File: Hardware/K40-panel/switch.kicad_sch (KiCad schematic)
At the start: 2 parts

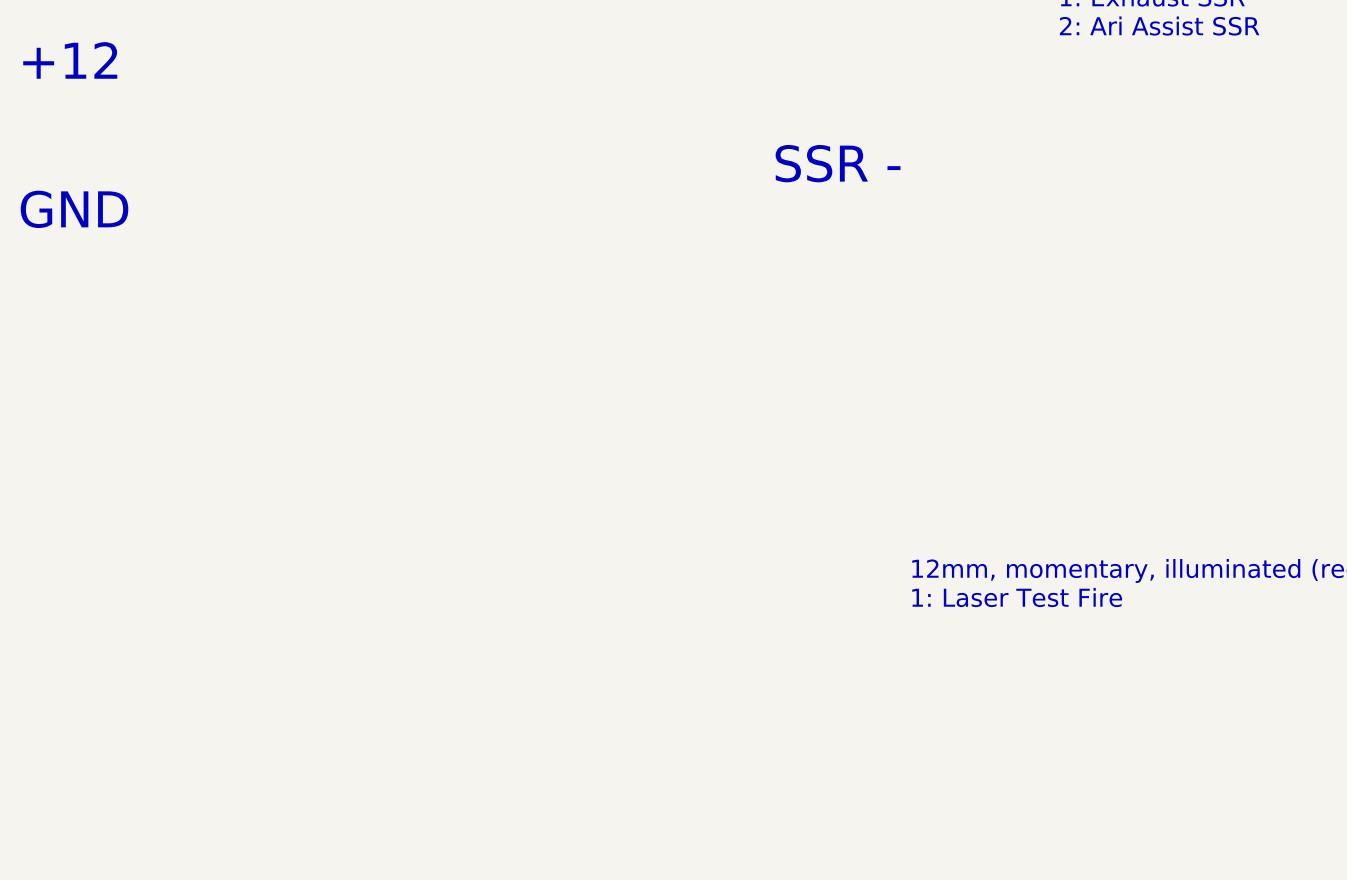
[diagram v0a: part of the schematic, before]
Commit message: modified:   Hardware/K40-panel/K40-panel.kicad_sch 	modified:   Hardware/K40-panel/switch.kicad_sch Updated labels 	modified:   Hardware/K40-power/K40-power.kicad_sch CLeaned up auxillary power diagram
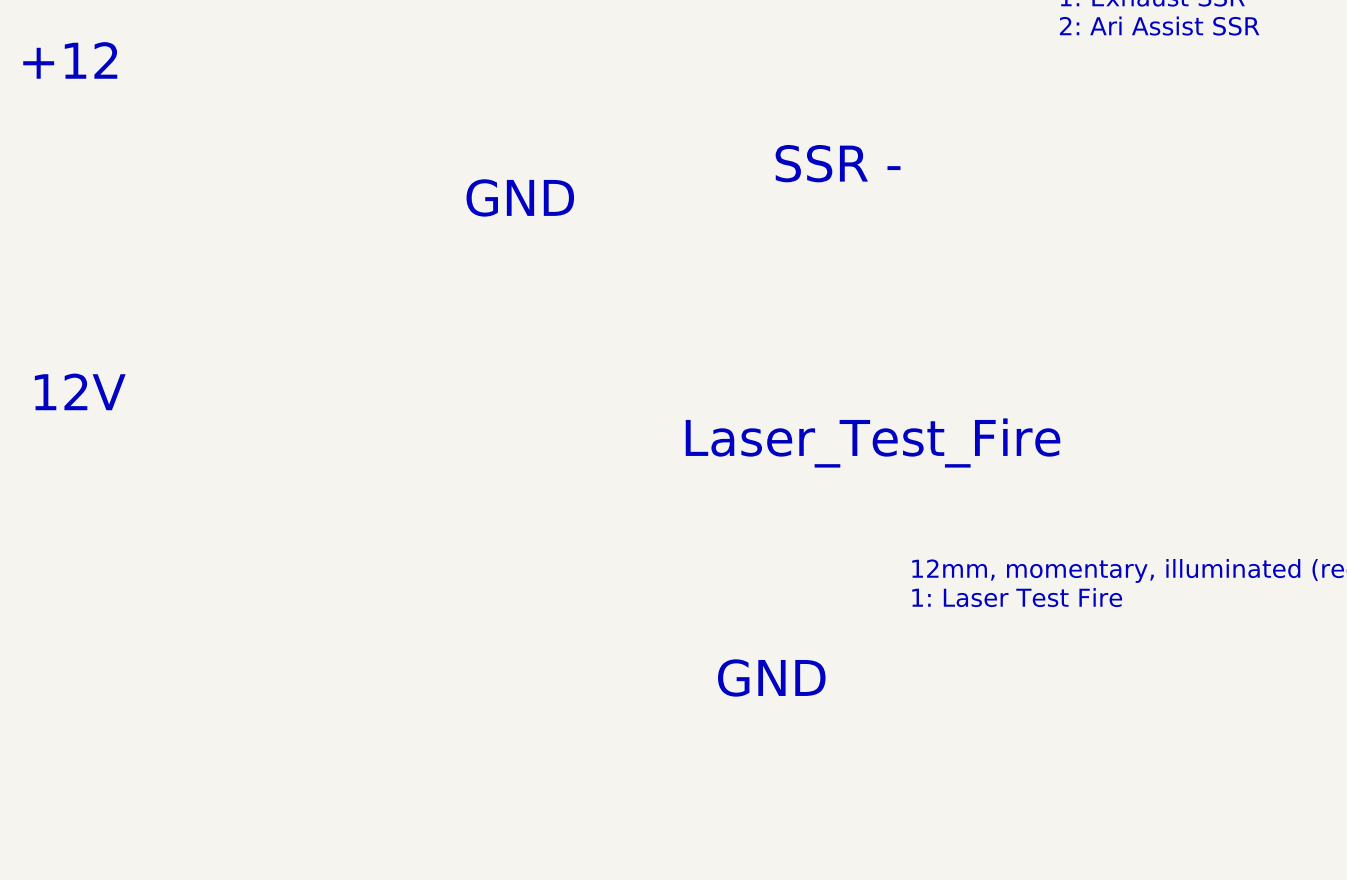
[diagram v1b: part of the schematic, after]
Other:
- note added: "12V"
- note added: "Laser_Test_Fire"

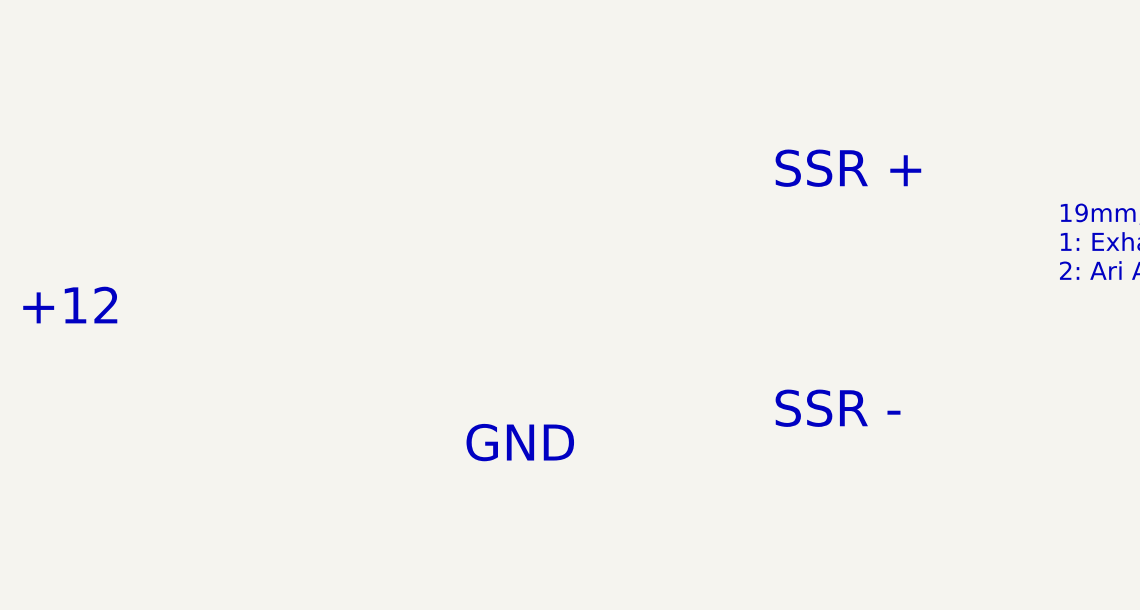
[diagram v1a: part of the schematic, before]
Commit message: Updated switch wiring on front panel
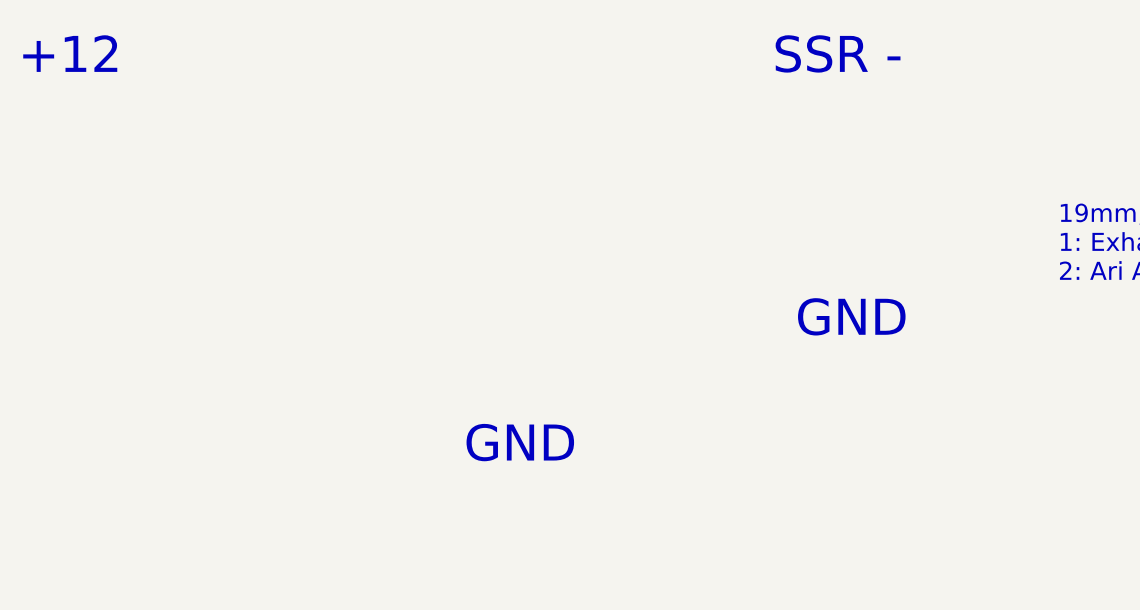
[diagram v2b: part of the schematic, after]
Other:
- note removed: "SSR +"
